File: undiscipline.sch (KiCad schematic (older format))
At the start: 168 parts, among them J1 Conn_01x04_Male, J2 USB_B_Micro, J3 Conn_01x02_Male, J4 Conn_01x02_Male, SW1 SW_Push, SW10 SW_Push, SW11 SW_Push, SW12 SW_Push, SW13 SW_Push, SW14 SW_Push, SW15 SW_Push, SW16 SW_Push, SW17 SW_Push, SW18 SW_Push, SW19 SW_Push, SW2 SW_Push, SW20 SW_Push, SW21 SW_Push, SW22 SW_Push, SW23 SW_Push, SW24 SW_Push, SW25 SW_Push, SW26 SW_Push, SW27 SW_Push, SW28 SW_Push, SW29 SW_Push, SW3 SW_Push, SW30 SW_Push, SW31 SW_Push, SW32 SW_Push, SW33 SW_Push, SW34 SW_Push, SW35 SW_Push, SW36 SW_Push, SW37 SW_Push, SW38 SW_Push, SW39 SW_Push, SW4 SW_Push, SW40 SW_Push, SW41 SW_Push, SW42 SW_Push, SW43 SW_Push, SW44 SW_Push, SW45 SW_Push, SW46 SW_Push, SW47 SW_Push, SW48 SW_Push, SW49 SW_Push, SW5 SW_Push, SW50 SW_Push, SW51 SW_Push, SW52 SW_Push, SW53 SW_Push, SW54 SW_Push, SW55 SW_Push, SW56 SW_Push, SW57 SW_Push, SW58 SW_Push, SW59 SW_Push, SW6 SW_Push, SW60 SW_Push, SW61 SW_Push, SW62 SW_Push, SW63 SW_Push, SW64 SW_Push, SW65 SW_Push, SW66 SW_Push, SW67 SW_Push, SW68 SW_Push, SW69 SW_Push, SW7 SW_Push, SW70 SW_Push, SW71 SW_Push, SW72 SW_Push, SW73 SW_Push, SW74 SW_Push, SW75 SW_Push, SW8 SW_Push, SW9 SW_Push, U1 ATmega32A-PU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

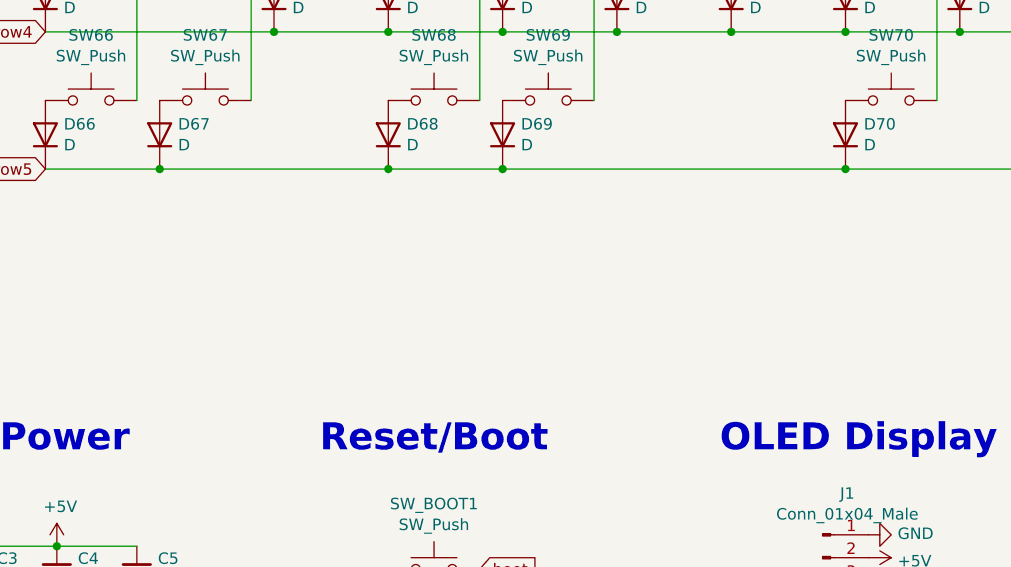
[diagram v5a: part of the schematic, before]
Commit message: Add mounting holes; move some tracks
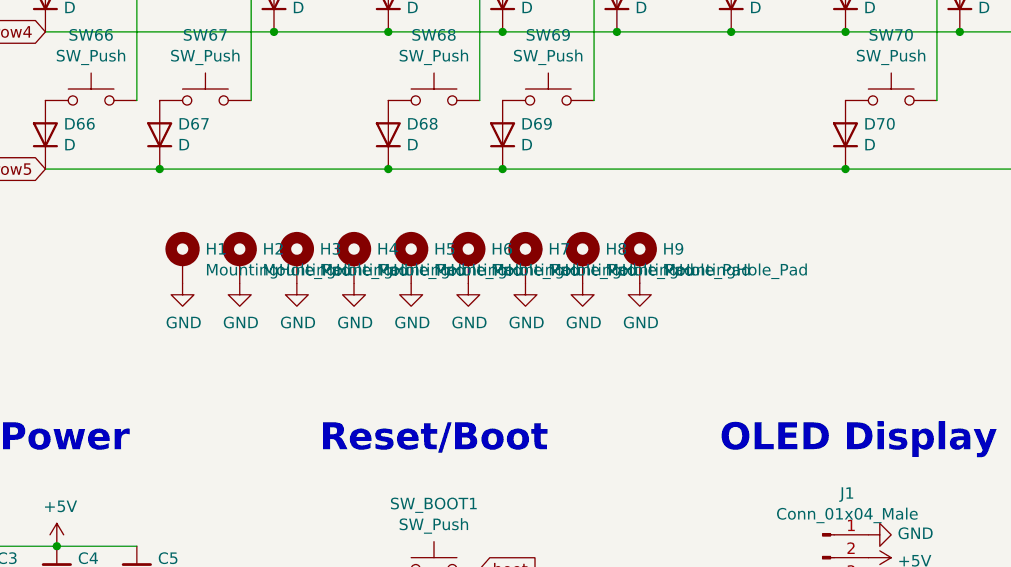
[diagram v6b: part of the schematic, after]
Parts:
- added H1, H2, H3, H4, H5, H6, H7, H8, H9: MountingHole_Pad, MountingHole:MountingHole_2.2mm_M2_DIN965_Pad_TopBottom, symbol Mechanical:MountingHole_Pad
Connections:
- net GND: now also H1.1, H2.1, H3.1, H4.1, H5.1, H6.1, H7.1, H8.1, H9.1
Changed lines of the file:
@@
+	1    0    0    -1
+$EndComp
+$Comp
+L Mechanical:MountingHole_Pad H1
+U 1 1 5FEA9D6F
+P 3700 4550
+F 0 "H1" H 3800 4599 50  0000 L CNN
+F 1 "MountingHole_Pad" H 3800 4508 50  0000 L CNN
+F 2 "MountingHole:MountingHole_2.2mm_M2_DIN965_Pad_TopBottom" H 3700 4550 50  0001 C CNN
+F 3 "~" H 3700 4550 50  0001 C CNN
+	1    3700 4550
+	1    0    0    -1
+$EndComp
+$Comp
+L power:GND #PWR022
+U 1 1 5FEAE1F9
+P 3700 4650
+F 0 "#PWR022" H 3700 4400 50  0001 C CNN
+F 1 "GND" H 3705 4477 50  0000 C CNN
+F 2 "" H 3700 4650 50  0001 C CNN
+F 3 "" H 3700 4650 50  0001 C CNN
+	1    3700 4650
+	1    0    0    -1
+$EndComp
+$Comp
+L Mechanical:MountingHole_Pad H2
+U 1 1 5FEB970A
+P 3950 4550
+F 0 "H2" H 4050 4599 50  0000 L CNN
+F 1 "MountingHole_Pad" H 4050 4508 50  0000 L CNN
+F 2 "MountingHole:MountingHole_2.2mm_M2_DIN965_Pad_TopBottom" H 3950 4550 50  0001 C CNN
+F 3 "~" H 3950 4550 50  0001 C CNN
+	1    3950 4550
+	1    0    0    -1
+$EndComp
+$Comp
+L power:GND #PWR023
+U 1 1 5FEB9710
+P 3950 4650
+F 0 "#PWR023" H 3950 4400 50  0001 C CNN
+F 1 "GND" H 3955 4477 50  0000 C CNN
+F 2 "" H 3950 4650 50  0001 C CNN
+F 3 "" H 3950 4650 50  0001 C CNN
+	1    3950 4650
+	1    0    0    -1
+$EndComp
+$Comp
+L Mechanical:MountingHole_Pad H3
+U 1 1 5FEC3930
+P 4200 4550
+F 0 "H3" H 4300 4599 50  0000 L CNN
+F 1 "MountingHole_Pad" H 4300 4508 50  0000 L CNN
+F 2 "MountingHole:MountingHole_2.2mm_M2_DIN965_Pad_TopBottom" H 4200 4550 50  0001 C CNN
+F 3 "~" H 4200 4550 50  0001 C CNN
+	1    4200 4550
+	1    0    0    -1
+$EndComp
+$Comp
+L power:GND #PWR024
+U 1 1 5FEC3936
+P 4200 4650
+F 0 "#PWR024" H 4200 4400 50  0001 C CNN
+F 1 "GND" H 4205 4477 50  0000 C CNN
+F 2 "" H 4200 4650 50  0001 C CNN
+F 3 "" H 4200 4650 50  0001 C CNN
+	1    4200 4650
+	1    0    0    -1
+$EndComp
+$Comp
+L Mechanical:MountingHole_Pad H4
+U 1 1 5FEC393C
+P 4450 4550
+F 0 "H4" H 4550 4599 50  0000 L CNN
+F 1 "MountingHole_Pad" H 4550 4508 50  0000 L CNN
+F 2 "MountingHole:MountingHole_2.2mm_M2_DIN965_Pad_TopBottom" H 4450 4550 50  0001 C CNN
+F 3 "~" H 4450 4550 50  0001 C CNN
+	1    4450 4550
+	1    0    0    -1
+$EndComp
+$Comp
+L power:GND #PWR025
+U 1 1 5FEC3942
+P 4450 4650
+F 0 "#PWR025" H 4450 4400 50  0001 C CNN
+F 1 "GND" H 4455 4477 50  0000 C CNN
+F 2 "" H 4450 4650 50  0001 C CNN
+F 3 "" H 4450 4650 50  0001 C CNN
+	1    4450 4650
+	1    0    0    -1
+$EndComp
+$Comp
+L Mechanical:MountingHole_Pad H5
+U 1 1 5FECE81A
+P 4700 4550
+F 0 "H5" H 4800 4599 50  0000 L CNN
+F 1 "MountingHole_Pad" H 4800 4508 50  0000 L CNN
+F 2 "MountingHole:MountingHole_2.2mm_M2_DIN965_Pad_TopBottom" H 4700 4550 50  0001 C CNN
+F 3 "~" H 4700 4550 50  0001 C CNN
+	1    4700 4550
+	1    0    0    -1
+$EndComp
+$Comp
+L power:GND #PWR026
+U 1 1 5FECE820
+P 4700 4650
+F 0 "#PWR026" H 4700 4400 50  0001 C CNN
+F 1 "GND" H 4705 4477 50  0000 C CNN
+F 2 "" H 4700 4650 50  0001 C CNN
+F 3 "" H 4700 4650 50  0001 C CNN
+	1    4700 4650
+	1    0    0    -1
+$EndComp
+$Comp
+L Mechanical:MountingHole_Pad H6
+U 1 1 5FECE826
+P 4950 4550
+F 0 "H6" H 5050 4599 50  0000 L CNN
+F 1 "MountingHole_Pad" H 5050 4508 50  0000 L CNN
+F 2 "MountingHole:MountingHole_2.2mm_M2_DIN965_Pad_TopBottom" H 4950 4550 50  0001 C CNN
+F 3 "~" H 4950 4550 50  0001 C CNN
+	1    4950 4550
+	1    0    0    -1
+$EndComp
+$Comp
+L power:GND #PWR027
+U 1 1 5FECE82C
+P 4950 4650
+F 0 "#PWR027" H 4950 4400 50  0001 C CNN
+F 1 "GND" H 4955 4477 50  0000 C CNN
+F 2 "" H 4950 4650 50  0001 C CNN
+F 3 "" H 4950 4650 50  0001 C CNN
+	1    4950 4650
+	1    0    0    -1
+$EndComp
+$Comp
+L Mechanical:MountingHole_Pad H7
+U 1 1 5FECE832
+P 5200 4550
+F 0 "H7" H 5300 4599 50  0000 L CNN
+F 1 "MountingHole_Pad" H 5300 4508 50  0000 L CNN
+F 2 "MountingHole:MountingHole_2.2mm_M2_DIN965_Pad_TopBottom" H 5200 4550 50  0001 C CNN
+F 3 "~" H 5200 4550 50  0001 C CNN
+	1    5200 4550
+	1    0    0    -1
+$EndComp
+$Comp
+L power:GND #PWR028
+U 1 1 5FECE838
+P 5200 4650
+F 0 "#PWR028" H 5200 4400 50  0001 C CNN
+F 1 "GND" H 5205 4477 50  0000 C CNN
+F 2 "" H 5200 4650 50  0001 C CNN
+F 3 "" H 5200 4650 50  0001 C CNN
+	1    5200 4650
+	1    0    0    -1
+$EndComp
+$Comp
+L Mechanical:MountingHole_Pad H8
+U 1 1 5FECE83E
+P 5450 4550
+F 0 "H8" H 5550 4599 50  0000 L CNN
+F 1 "MountingHole_Pad" H 5550 4508 50  0000 L CNN
+F 2 "MountingHole:MountingHole_2.2mm_M2_DIN965_Pad_TopBottom" H 5450 4550 50  0001 C CNN
+F 3 "~" H 5450 4550 50  0001 C CNN
+	1    5450 4550
+	1    0    0    -1
+$EndComp
+$Comp
+L power:GND #PWR029
+U 1 1 5FECE844
+P 5450 4650
+F 0 "#PWR029" H 5450 4400 50  0001 C CNN
+F 1 "GND" H 5455 4477 50  0000 C CNN
+F 2 "" H 5450 4650 50  0001 C CNN
+F 3 "" H 5450 4650 50  0001 C CNN
+	1    5450 4650
+	1    0    0    -1
+$EndComp
+$Comp
+L Mechanical:MountingHole_Pad H9
+U 1 1 5FF5DF9F
+P 5700 4550
+F 0 "H9" H 5800 4599 50  0000 L CNN
+F 1 "MountingHole_Pad" H 5800 4508 50  0000 L CNN
+F 2 "MountingHole:MountingHole_2.2mm_M2_DIN965_Pad_TopBottom" H 5700 4550 50  0001 C CNN
+F 3 "~" H 5700 4550 50  0001 C CNN
+	1    5700 4550
+	1    0    0    -1
+$EndComp
+$Comp
+L power:GND #PWR030
+U 1 1 5FF5DFA5
+P 5700 4650
+F 0 "#PWR030" H 5700 4400 50  0001 C CNN
+F 1 "GND" H 5705 4477 50  0000 C CNN
+F 2 "" H 5700 4650 50  0001 C CNN
+F 3 "" H 5700 4650 50  0001 C CNN
+	1    5700 4650
 	1    0    0    -1
 $EndComp

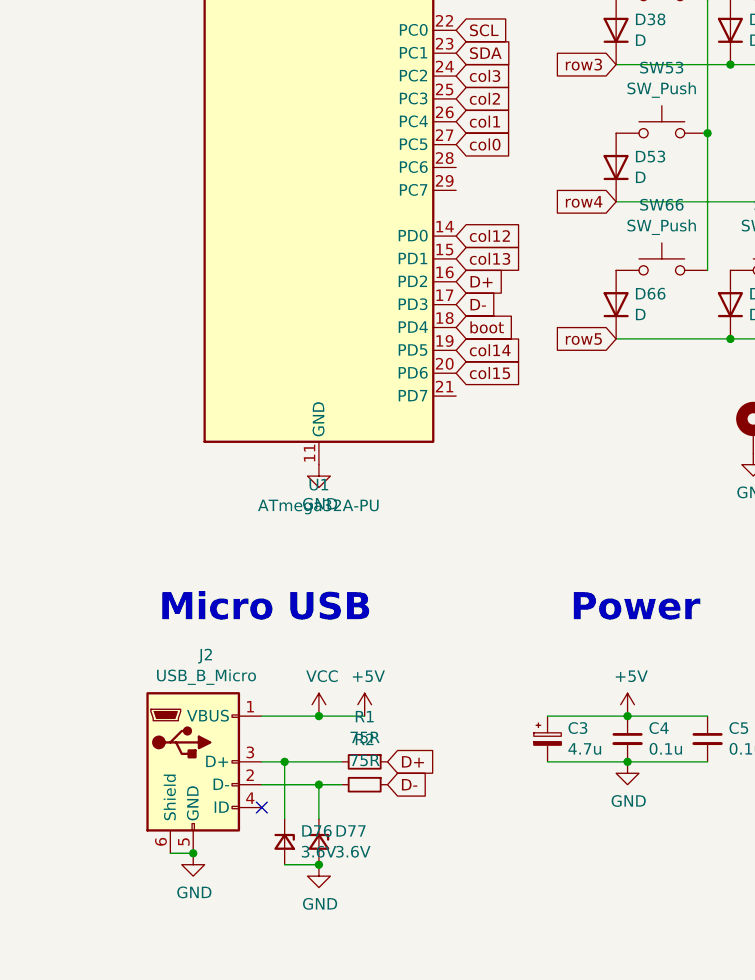
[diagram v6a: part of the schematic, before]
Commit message: Move PCB references
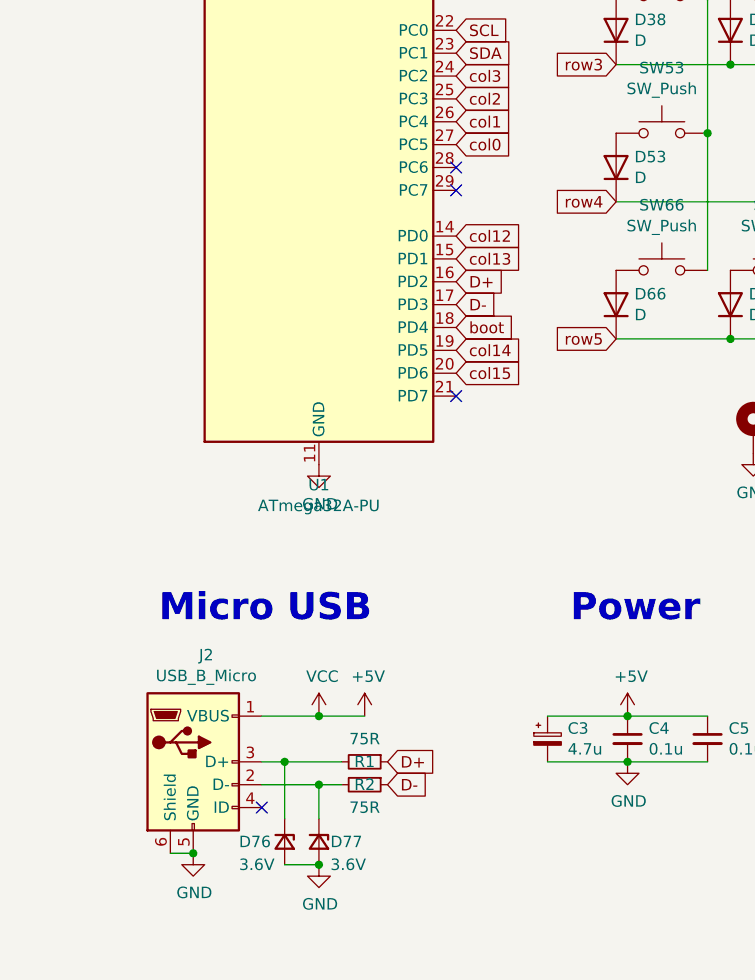
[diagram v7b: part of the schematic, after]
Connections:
- no-connect marks 3 -> 6
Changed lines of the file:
@@
 U 1 1 600A4A74
 P 2000 6000
-F 0 "R1" V 1804 6000 50  0000 C CNN
-F 1 "75R" V 1895 6000 50  0000 C CNN
+F 0 "R1" V 2000 6000 50  0000 C CNN
+F 1 "75R" V 1900 6000 50  0000 C CNN
 F 2 "Resistor_THT:R_Axial_DIN0204_L3.6mm_D1.6mm_P5.08mm_Horizontal" H 2000 6000 50  0001 C CNN
 F 3 "~" H 2000 6000 50  0001 C CNN
@@
 U 1 1 600B99AC
 P 2000 6100
-F 0 "R2" V 1804 6100 50  0000 C CNN
-F 1 "75R" V 1895 6100 50  0000 C CNN
+F 0 "R2" V 2000 6100 50  0000 C CNN
+F 1 "75R" V 2100 6100 50  0000 C CNN
 F 2 "Resistor_THT:R_Axial_DIN0204_L3.6mm_D1.6mm_P5.08mm_Horizontal" H 2000 6100 50  0001 C CNN
 F 3 "~" H 2000 6100 50  0001 C CNN
@@
 U 1 1 60149C80
 P 1650 6350
-F 0 "D76" V 1604 6420 50  0000 L CNN
-F 1 "3.6V" V 1695 6420 50  0000 L CNN
+F 0 "D76" V 1650 6150 50  0000 L CNN
+F 1 "3.6V" V 1750 6150 50  0000 L CNN
 F 2 "Diode_THT:D_T-1_P5.08mm_Horizontal" V 1650 6350 50  0001 C CNN
 F 3 "~" V 1650 6350 50  0001 C CNN
@@
 U 1 1 60151106
 P 1800 6350
-F 0 "D77" V 1754 6420 50  0000 L CNN
-F 1 "3.6V" V 1845 6420 50  0000 L CNN
+F 0 "D77" V 1800 6400 50  0000 L CNN
+F 1 "3.6V" V 1900 6400 50  0000 L CNN
 F 2 "Diode_THT:D_T-1_P5.08mm_Horizontal" V 1800 6350 50  0001 C CNN
 F 3 "~" V 1800 6350 50  0001 C CNN
@@
 	1    0    0    -1
 $EndComp
+NoConn ~ 2400 3400
+NoConn ~ 2400 3500
+NoConn ~ 2400 4400
 $EndSCHEMATC

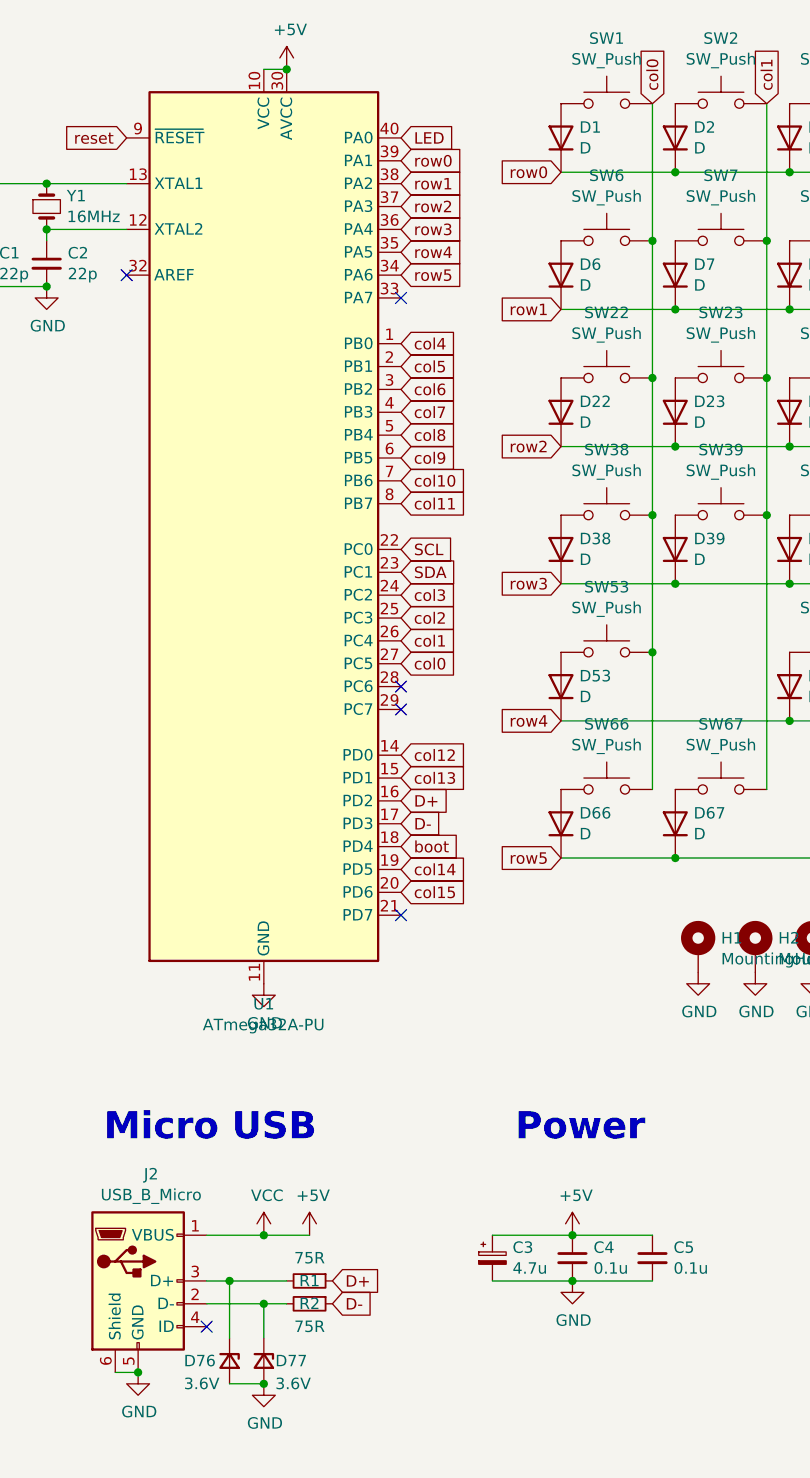
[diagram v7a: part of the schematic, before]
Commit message: Improve GND stiching
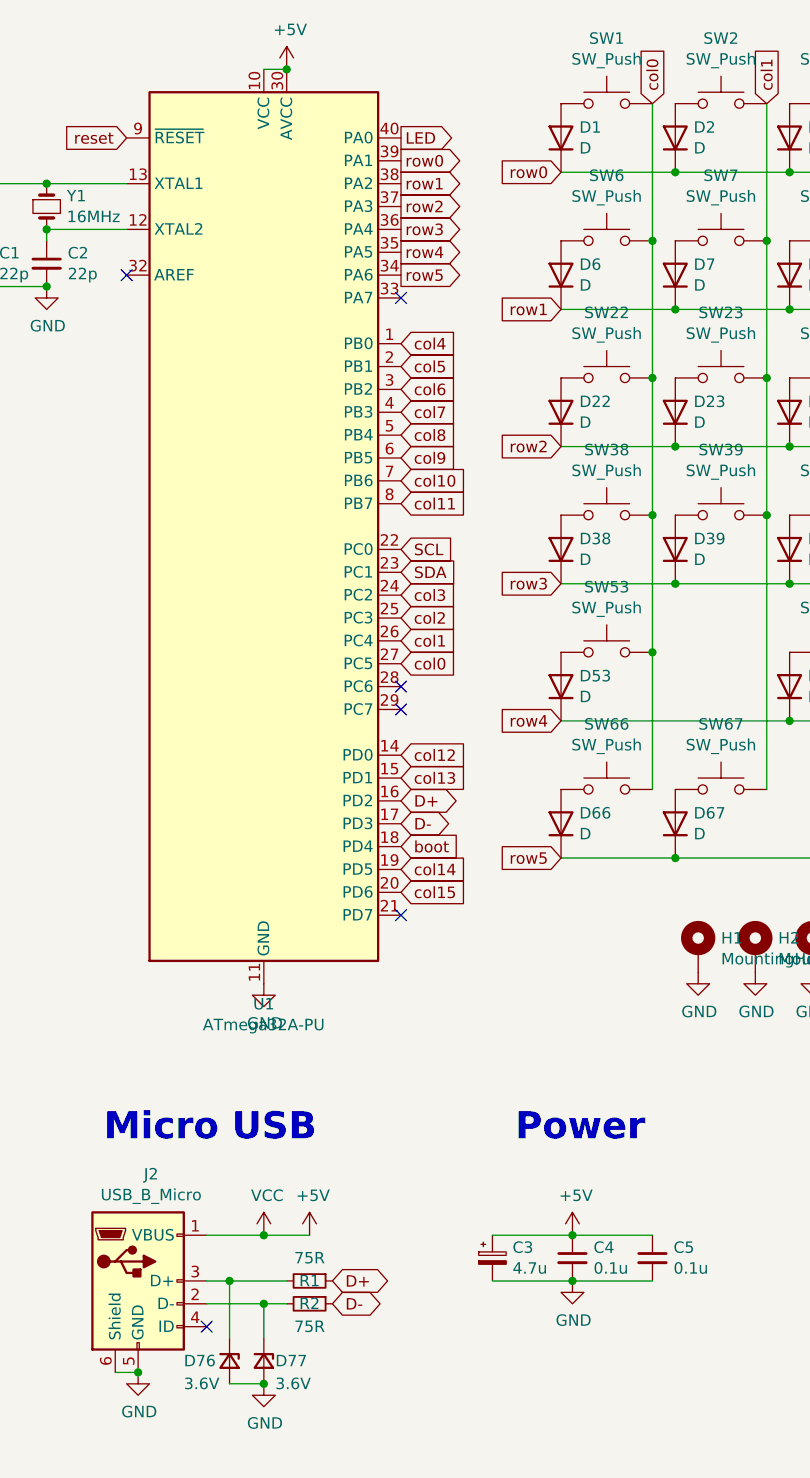
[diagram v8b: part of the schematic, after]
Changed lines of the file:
@@
 Text GLabel 10500 1450 1    50   Input ~ 0
 col14
-Text GLabel 3100 1150 0    50   Input ~ 0
-row0
 Text GLabel 3100 1750 0    50   Input ~ 0
 row1
@@
 	1    0    0    -1
 $EndComp
-Text GLabel 2100 6000 2    50   Input ~ 0
+Text GLabel 2100 6000 2    50   BiDi ~ 0
 D+
-Text GLabel 2100 6100 2    50   Input ~ 0
+Text GLabel 2100 6100 2    50   BiDi ~ 0
 D-
 NoConn ~ 1550 6200
@@
 $EndComp
 Connection ~ 1900 700
-Text GLabel 2400 1400 2    50   Input ~ 0
+Text GLabel 2400 1400 2    50   Output ~ 0
 row3
-Text GLabel 2400 1200 2    50   Input ~ 0
+Text GLabel 2400 1200 2    50   Output ~ 0
 row1
 Text GLabel 2400 3300 2    50   Input ~ 0
@@
 col4
 NoConn ~ 2400 1700
-Text GLabel 2400 1500 2    50   Input ~ 0
+Text GLabel 2400 1500 2    50   Output ~ 0
 row4
-Text GLabel 2400 1300 2    50   Input ~ 0
+Text GLabel 2400 1300 2    50   Output ~ 0
 row2
-Text GLabel 2400 1100 2    50   Input ~ 0
+Text GLabel 2400 1100 2    50   Output ~ 0
 row0
 Text GLabel 2400 3200 2    50   Input ~ 0
@@
 Text GLabel 2400 2200 2    50   Input ~ 0
 col7
-Text GLabel 2400 3900 2    50   Input ~ 0
+Text GLabel 2400 3900 2    50   BiDi ~ 0
 D+
-Text GLabel 2400 4000 2    50   Input ~ 0
+Text GLabel 2400 4000 2    50   BiDi ~ 0
 D-
 Text GLabel 2400 4100 2    50   Input ~ 0
@@
 Text GLabel 2400 2900 2    50   Input ~ 0
 SDA
-Text GLabel 2400 1600 2    50   Input ~ 0
+Text GLabel 2400 1600 2    50   Output ~ 0
 row5
 $Comp
@@
 F2 "LED" I R 8900 4900 50
 $EndSheet
-Text GLabel 2400 1000 2    50   Input ~ 0
+Text GLabel 2400 1000 2    50   Output ~ 0
 LED
 Text GLabel 8900 4900 2    50   Input ~ 0
@@
 NoConn ~ 2400 3500
 NoConn ~ 2400 4400
+Text GLabel 3100 1150 0    50   Input ~ 0
+row0
 $EndSCHEMATC
